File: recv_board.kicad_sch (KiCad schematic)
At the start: 24 parts

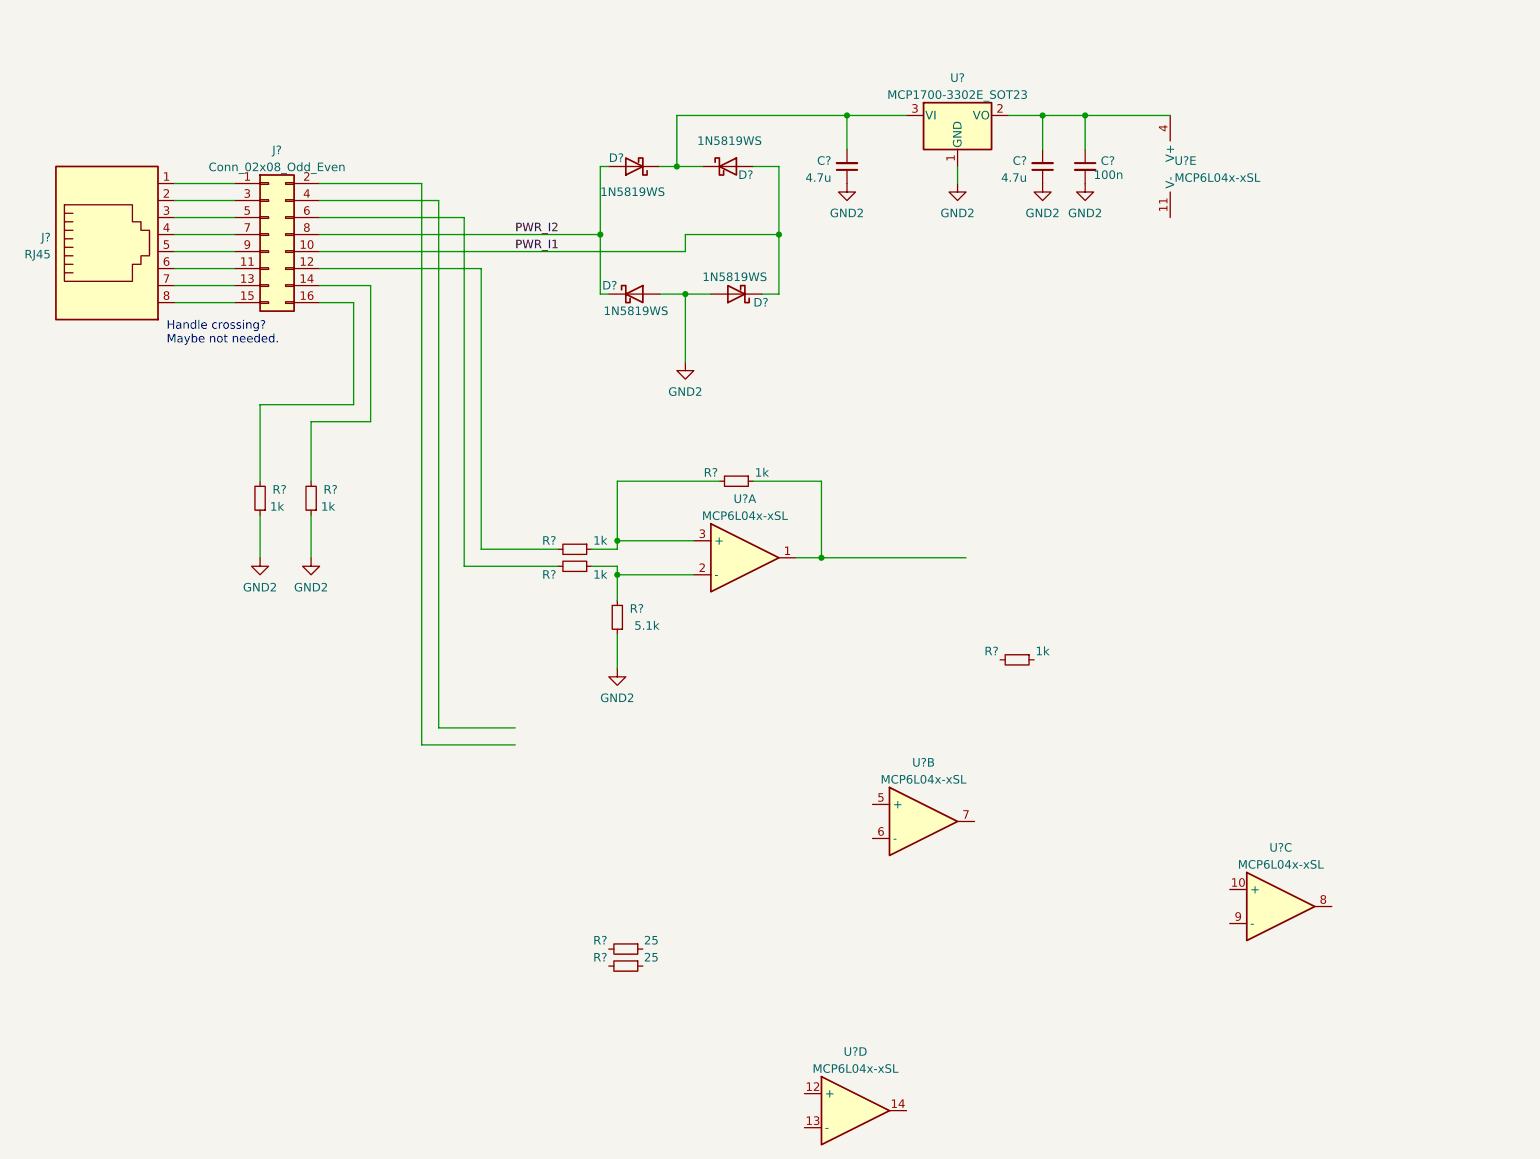
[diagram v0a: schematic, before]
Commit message: finish schematic, add cubemx project, some initial layout
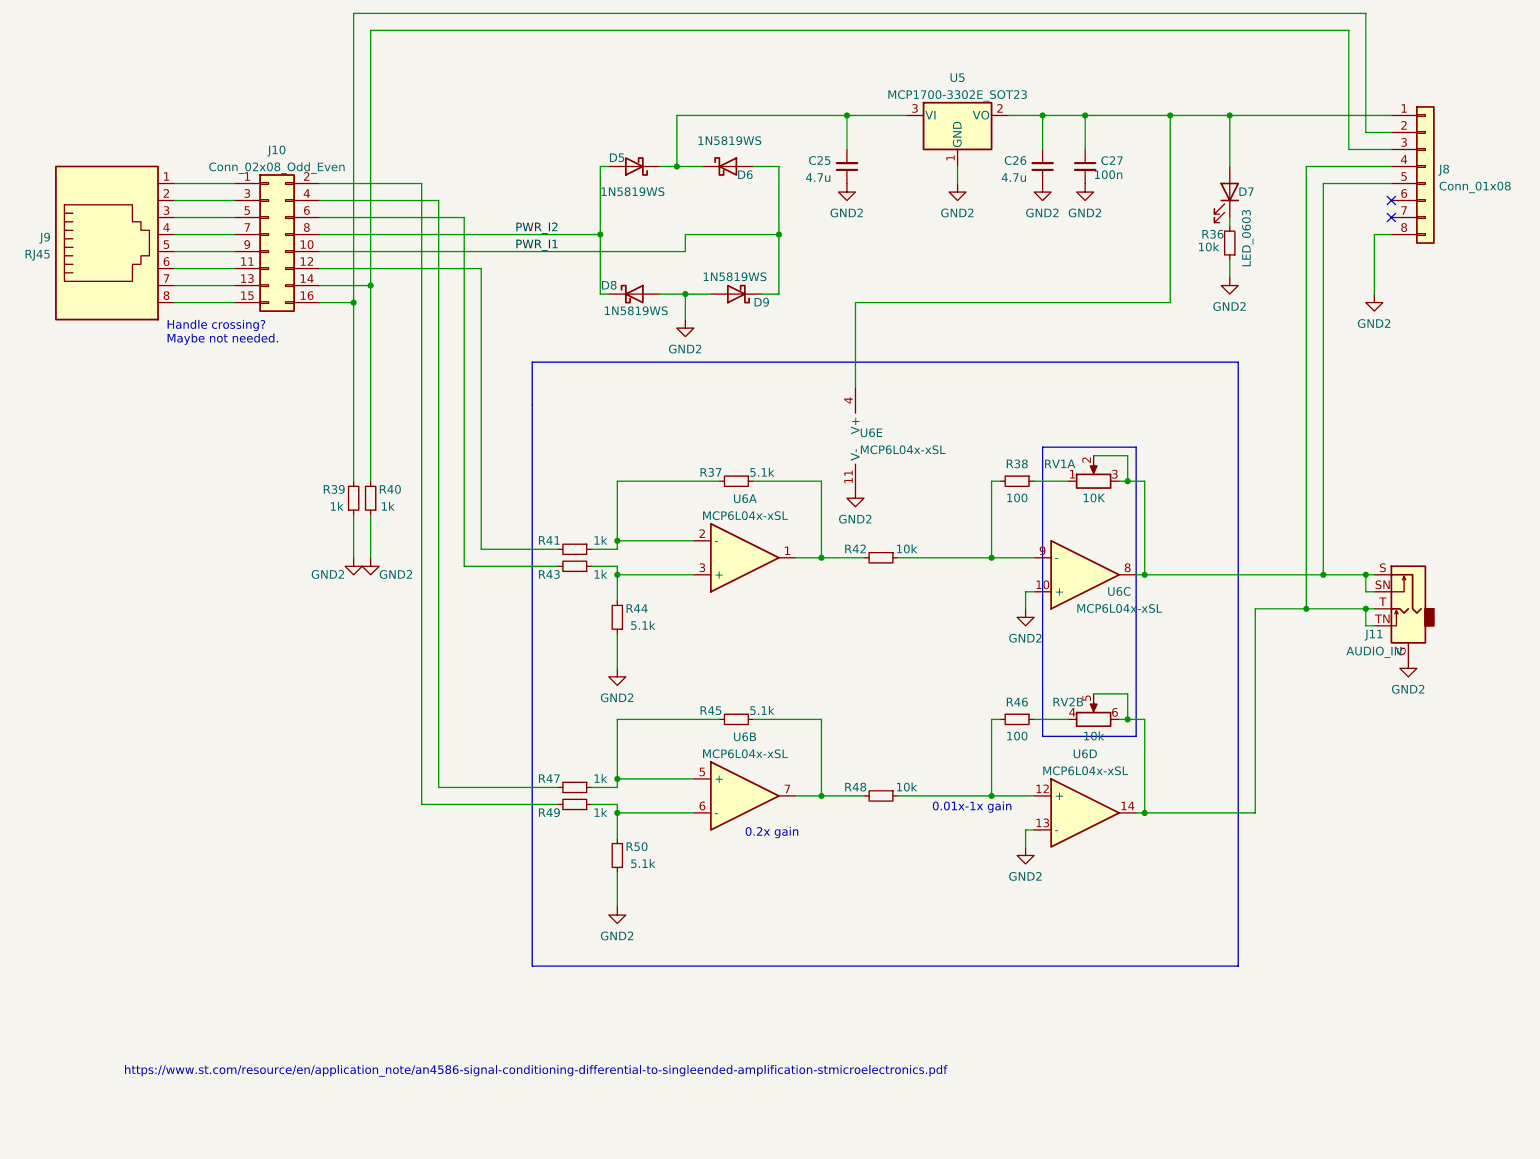
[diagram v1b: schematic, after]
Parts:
- removed R? (x2): 25, Resistor_SMD:R_0603_1608Metric_Pad0.98x0.95mm_HandSolder, symbol Device:R_Small
- removed R?: 1k, Resistor_SMD:R_0603_1608Metric_Pad0.98x0.95mm_HandSolder, symbol Device:R_Small
- added D7: LED_0603, LED_SMD:LED_0603_1608Metric_Pad1.05x0.95mm_HandSolder, symbol Device:LED
- added J11: AUDIO_IN, Connector_Audio:Jack_3.5mm_CUI_SJ1-3535NG_Horizontal_CircularHoles, symbol Connector:AudioJack2_Ground_Switch
- added J8: Conn_01x08, Connector_PinHeader_2.54mm:PinHeader_1x08_P2.54mm_Vertical, symbol Connector_Generic:Conn_01x08
- added R36, R42, R48: 10k, Resistor_SMD:R_0402_1005Metric, symbol Device:R_Small
- added R38, R46: 100, Resistor_SMD:R_0402_1005Metric, symbol Device:R_Small
- added R45, R50: 5.1k, Resistor_SMD:R_0402_1005Metric, symbol Device:R_Small
- added R47, R49: 1k, Resistor_SMD:R_0402_1005Metric, symbol Device:R_Small
- added RV1: 10K, Potentiometer_THT:Potentiometer_Alps_RK163_Dual_Horizontal, symbol Device:R_Potentiometer_Dual_Separate
- added RV2: 10k, Potentiometer_THT:Potentiometer_Alps_RK163_Dual_Horizontal, symbol Device:R_Potentiometer_Dual_Separate
- J10: renamed from J?; footprint (none) -> Connector_PinSocket_2.54mm:PinSocket_2x08_P2.54mm_Vertical
- J9: renamed from J?; footprint (none) -> Connector_RJ:RJ45_OST_PJ012-8P8CX_Vertical
- R37: renamed from R?; value 1k -> 5.1k; footprint Resistor_SMD:R_0603_1608Metric_Pad0.98x0.95mm_HandSolder -> Resistor_SMD:R_0402_1005Metric
- R39, R40, R41, R43, R44: renamed from R?; footprint Resistor_SMD:R_0603_1608Metric_Pad0.98x0.95mm_HandSolder -> Resistor_SMD:R_0402_1005Metric
- gave numbers to parts that had none: 9
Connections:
- net GND2: now also U6.10 (+), U6.11 (V-), U6.13 (-), J11.G, J8.8 (Pin_8), R36.1, R50.1
- net at U6.12 (+): now also R46.2, R48.1
- net at U6.14: now also J11.T, J11.TN, J8.4 (Pin_4), RV2.5, RV2.6
- net at J10.16 (Pin_16), R39.2: now also J8.2 (Pin_2)
- net at C26.2, C27.1, U5.2 (VO)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: now also D7.2 (A), J8.1 (Pin_1)
- net at U6.8: now also J11.S, J11.SN, J8.5 (Pin_5), RV1.2, RV1.3
- net at U6.9 (-): now also R38.2, R42.1
- net at R37.2, R41.1: now also U6.2 (-); no longer U6.3 (+)
- net at R43.1, R44.2: now also U6.3 (+); no longer U6.2 (-)
- net at R37.1, U6.1: now also R42.2
- net at J10.14 (Pin_14), R40.2: now also J8.3 (Pin_3)
- net at J10.2 (Pin_2): now also R49.2
- net at J10.4 (Pin_4): now also R47.2
- net at U6.5 (+): now also R45.2, R47.1
- net at U6.6 (-): now also R49.1, R50.2
- net at U6.7: now also R45.1, R48.2
- new net: R46.1, RV2.4
- new net: D7.1 (K), R36.2
- new net: R38.1, RV1.1
- no-connect marks 0 -> 2
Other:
- note added: "0.01x-1x gain"
- note added: "0.2x gain"
- note added: "https://www.st.com/resource/en/application_note/an4586-signal-conditioning-differential-to-singleended-amplification-stmicroelectronics.pdf"
- moved on the sheet: R39, R40, U6B, U6C, U6D, U6E
